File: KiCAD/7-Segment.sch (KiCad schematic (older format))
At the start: 26 parts, among them J1 3Pin_Fem, J2 3Pin_Male, J3 3Pin_Fem, J4 3Pin_Male, J5 3Pin_Fem, J6 3Pin_Male, J7 3Pin_Fem, J8 3Pin_Male

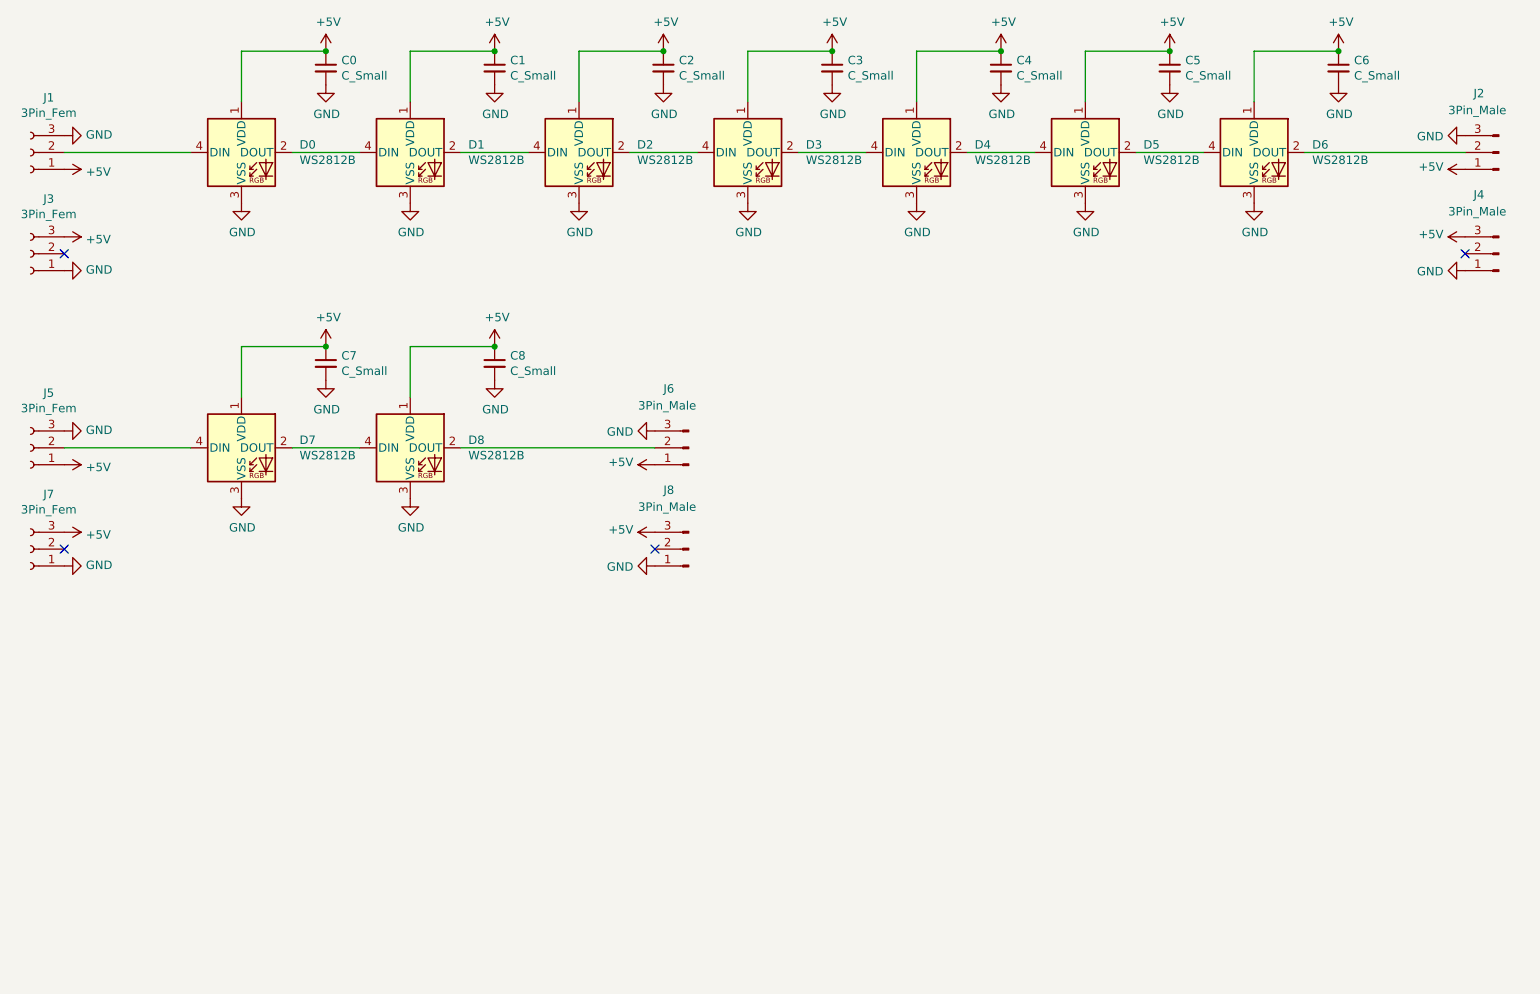
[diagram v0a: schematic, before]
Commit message: 2-LED per segment
Changed from 1 to 2 LEDs per segment. Removed caps per LED and included 2 placeholder caps for the module.
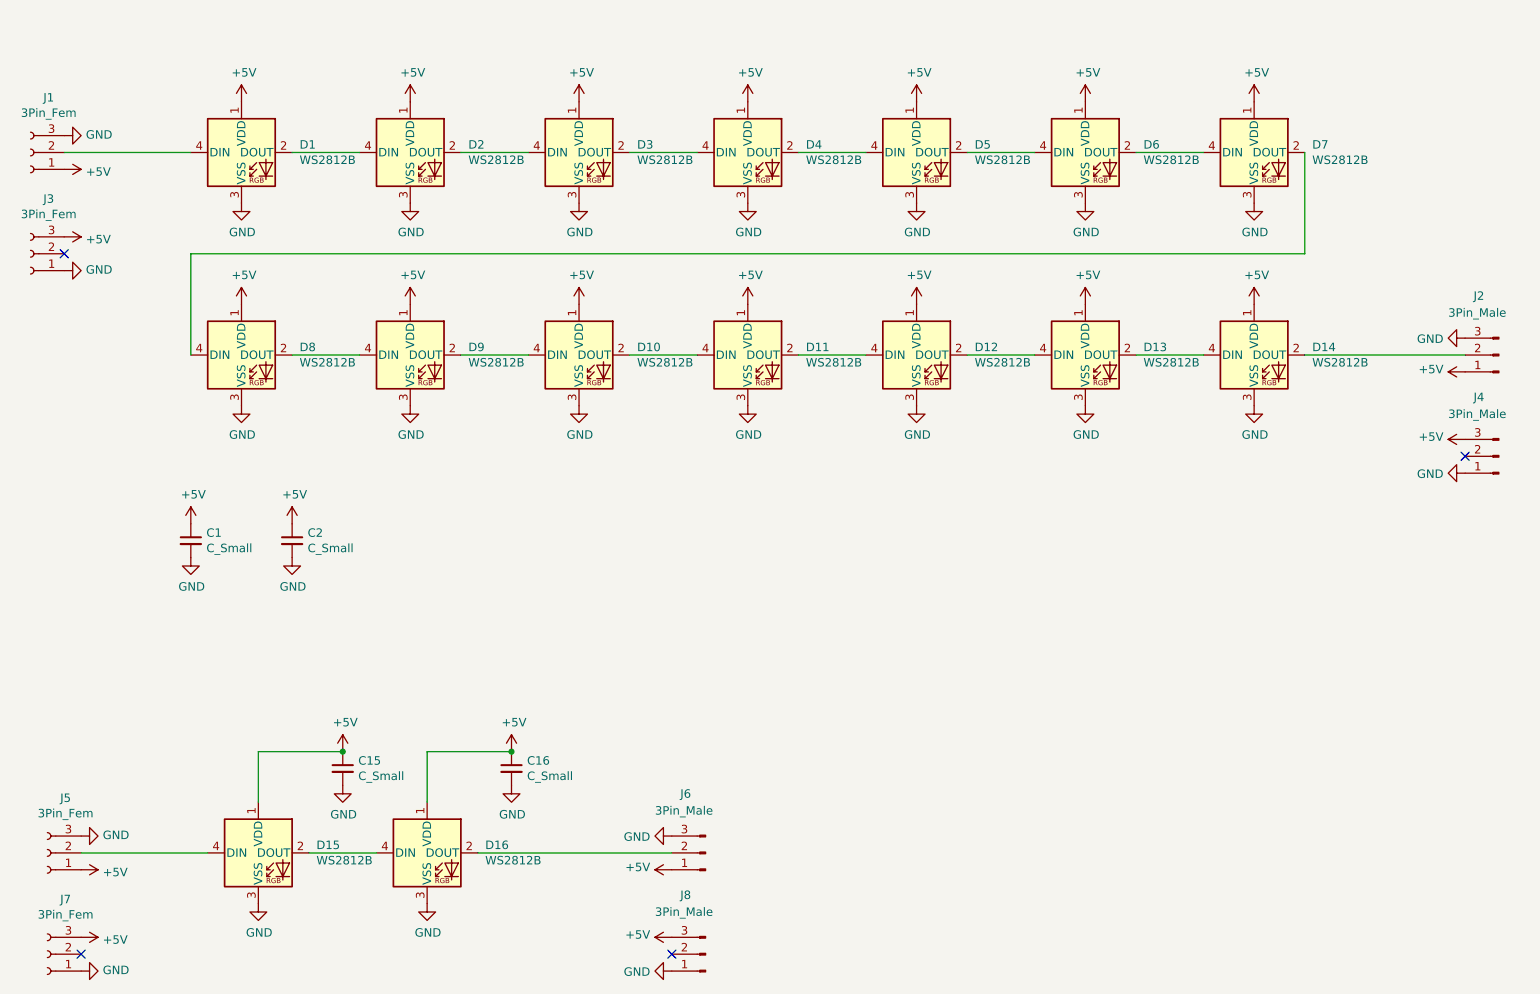
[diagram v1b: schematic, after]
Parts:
- removed C0, C3, C4, C5, C6: C_Small, Capacitors_SMD:C_0805, symbol Device:C_Small
- added D10, D11, D12, D13, D14, D8, D9: WS2812B, LEDs:LED_WS2812B-PLCC4, symbol LED:WS2812B
- renumbered C7 to C15, C8 to C16, D7 to D15, D8 to D16, D0 to D7
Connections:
- net +5V: now also D10.1 (VDD), D11.1 (VDD), D12.1 (VDD), D13.1 (VDD), D14.1 (VDD), D8.1 (VDD), D9.1 (VDD)
- net GND: now also D10.3 (VSS), D11.3 (VSS), D12.3 (VSS), D13.3 (VSS), D14.3 (VSS), D8.3 (VSS), D9.3 (VSS)
- net at D7.2 (DOUT): now also D8.4 (DIN); no longer D1.4 (DIN)
- net at D7.4 (DIN): now also D6.2 (DOUT); no longer J1.2 (Pin_2)
- net at J2.2 (Pin_2): now also D14.2 (DOUT); no longer D6.2 (DOUT)
- new net: D1.4 (DIN), J1.2 (Pin_2)
- new net: D13.2 (DOUT), D14.4 (DIN)
- new net: D8.2 (DOUT), D9.4 (DIN)
- new net: D10.4 (DIN), D9.2 (DOUT)
- new net: D10.2 (DOUT), D11.4 (DIN)
- new net: D11.2 (DOUT), D12.4 (DIN)
- new net: D12.2 (DOUT), D13.4 (DIN)
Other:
- moved on the sheet: C15, C16, D1, D15, D16, D2, D3, D4, D5, D6, D7, J2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

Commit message: Iterative updates
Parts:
- C1: value C_Small -> C_Big; footprint Capacitors_SMD:C_0805 -> Capacitors_SMD:CP_Elec_5x5.3
- C15, C16, C2: footprint Capacitors_SMD:C_0805 -> Capacitors_SMD:C_1206
- J1, J2, J3, J4, J5, J6, J7, J8: footprint 7-Segment Lib:Header3Pin_03 -> 7-Segment Lib:Header3Pin_04
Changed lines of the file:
@@
 F 0 "J2" H 10350 2500 50  0000 R CNN
 F 1 "3Pin_Male" H 10500 2600 50  0000 R CNN
-F 2 "7-Segment Lib:Header3Pin_03" H 10200 2850 50  0001 C CNN
+F 2 "7-Segment Lib:Header3Pin_04" H 10200 2850 50  0001 C CNN
 F 3 "~" H 10200 2850 50  0001 C CNN
 	1    10200 2850
@@
 F 0 "J1" H 1392 1325 50  0000 C CNN
 F 1 "3Pin_Fem" H 1392 1416 50  0000 C CNN
-F 2 "7-Segment Lib:Header3Pin_03" H 1500 1650 50  0001 C CNN
+F 2 "7-Segment Lib:Header3Pin_04" H 1500 1650 50  0001 C CNN
 F 3 "~" H 1500 1650 50  0001 C CNN
 	1    1500 1650
@@
 F 0 "J4" H 10350 3100 50  0000 R CNN
 F 1 "3Pin_Male" H 10500 3200 50  0000 R CNN
-F 2 "7-Segment Lib:Header3Pin_03" H 10200 3450 50  0001 C CNN
+F 2 "7-Segment Lib:Header3Pin_04" H 10200 3450 50  0001 C CNN
 F 3 "~" H 10200 3450 50  0001 C CNN
 	1    10200 3450
@@
 F 0 "J3" H 1392 1925 50  0000 C CNN
 F 1 "3Pin_Fem" H 1392 2016 50  0000 C CNN
-F 2 "7-Segment Lib:Header3Pin_03" H 1500 2250 50  0001 C CNN
+F 2 "7-Segment Lib:Header3Pin_04" H 1500 2250 50  0001 C CNN
 F 3 "~" H 1500 2250 50  0001 C CNN
 	1    1500 2250
@@
 F 0 "C15" H 3442 5346 50  0000 L CNN
 F 1 "C_Small" H 3442 5255 50  0000 L CNN
-F 2 "Capacitors_SMD:C_0805" H 3350 5300 50  0001 C CNN
+F 2 "Capacitors_SMD:C_1206" H 3350 5300 50  0001 C CNN
 F 3 "~" H 3350 5300 50  0001 C CNN
 	1    3350 5300
@@
 F 0 "C16" H 4442 5346 50  0000 L CNN
 F 1 "C_Small" H 4442 5255 50  0000 L CNN
-F 2 "Capacitors_SMD:C_0805" H 4350 5300 50  0001 C CNN
+F 2 "Capacitors_SMD:C_1206" H 4350 5300 50  0001 C CNN
 F 3 "~" H 4350 5300 50  0001 C CNN
 	1    4350 5300
@@
 F 0 "J6" H 5650 5450 50  0000 R CNN
 F 1 "3Pin_Male" H 5800 5550 50  0000 R CNN
-F 2 "7-Segment Lib:Header3Pin_03" H 5500 5800 50  0001 C CNN
+F 2 "7-Segment Lib:Header3Pin_04" H 5500 5800 50  0001 C CNN
 F 3 "~" H 5500 5800 50  0001 C CNN
 	1    5500 5800
@@
 F 0 "J5" H 1492 5475 50  0000 C CNN
 F 1 "3Pin_Fem" H 1492 5566 50  0000 C CNN
-F 2 "7-Segment Lib:Header3Pin_03" H 1600 5800 50  0001 C CNN
+F 2 "7-Segment Lib:Header3Pin_04" H 1600 5800 50  0001 C CNN
 F 3 "~" H 1600 5800 50  0001 C CNN
 	1    1600 5800
@@
 F 0 "J8" H 5650 6050 50  0000 R CNN
 F 1 "3Pin_Male" H 5800 6150 50  0000 R CNN
-F 2 "7-Segment Lib:Header3Pin_03" H 5500 6400 50  0001 C CNN
+F 2 "7-Segment Lib:Header3Pin_04" H 5500 6400 50  0001 C CNN
 F 3 "~" H 5500 6400 50  0001 C CNN
 	1    5500 6400
@@
 F 0 "J7" H 1492 6075 50  0000 C CNN
 F 1 "3Pin_Fem" H 1492 6166 50  0000 C CNN
-F 2 "7-Segment Lib:Header3Pin_03" H 1600 6400 50  0001 C CNN
+F 2 "7-Segment Lib:Header3Pin_04" H 1600 6400 50  0001 C CNN
 F 3 "~" H 1600 6400 50  0001 C CNN
 	1    1600 6400
@@
 P 2450 3950
 F 0 "C1" H 2542 3996 50  0000 L CNN
-F 1 "C_Small" H 2542 3905 50  0000 L CNN
-F 2 "Capacitors_SMD:C_0805" H 2450 3950 50  0001 C CNN
+F 1 "C_Big" H 2542 3905 50  0000 L CNN
+F 2 "Capacitors_SMD:CP_Elec_5x5.3" H 2450 3950 50  0001 C CNN
 F 3 "~" H 2450 3950 50  0001 C CNN
 	1    2450 3950
@@
 F 0 "C2" H 3142 3996 50  0000 L CNN
 F 1 "C_Small" H 3142 3905 50  0000 L CNN
-F 2 "Capacitors_SMD:C_0805" H 3050 3950 50  0001 C CNN
+F 2 "Capacitors_SMD:C_1206" H 3050 3950 50  0001 C CNN
 F 3 "~" H 3050 3950 50  0001 C CNN
 	1    3050 3950
